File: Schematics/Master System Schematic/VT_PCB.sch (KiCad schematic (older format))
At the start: 34 parts, among them K13 Voltage Tap Relay, K14 Voltage Tap Relay, K15 Voltage Tap Relay, K16 Voltage Tap Relay, K17 Voltage Tap Relay, K18 Voltage Tap Relay, K19 Voltage Tap Relay, K20 Voltage Tap Relay, K21 Voltage Tap Relay, K22 Voltage Tap Relay

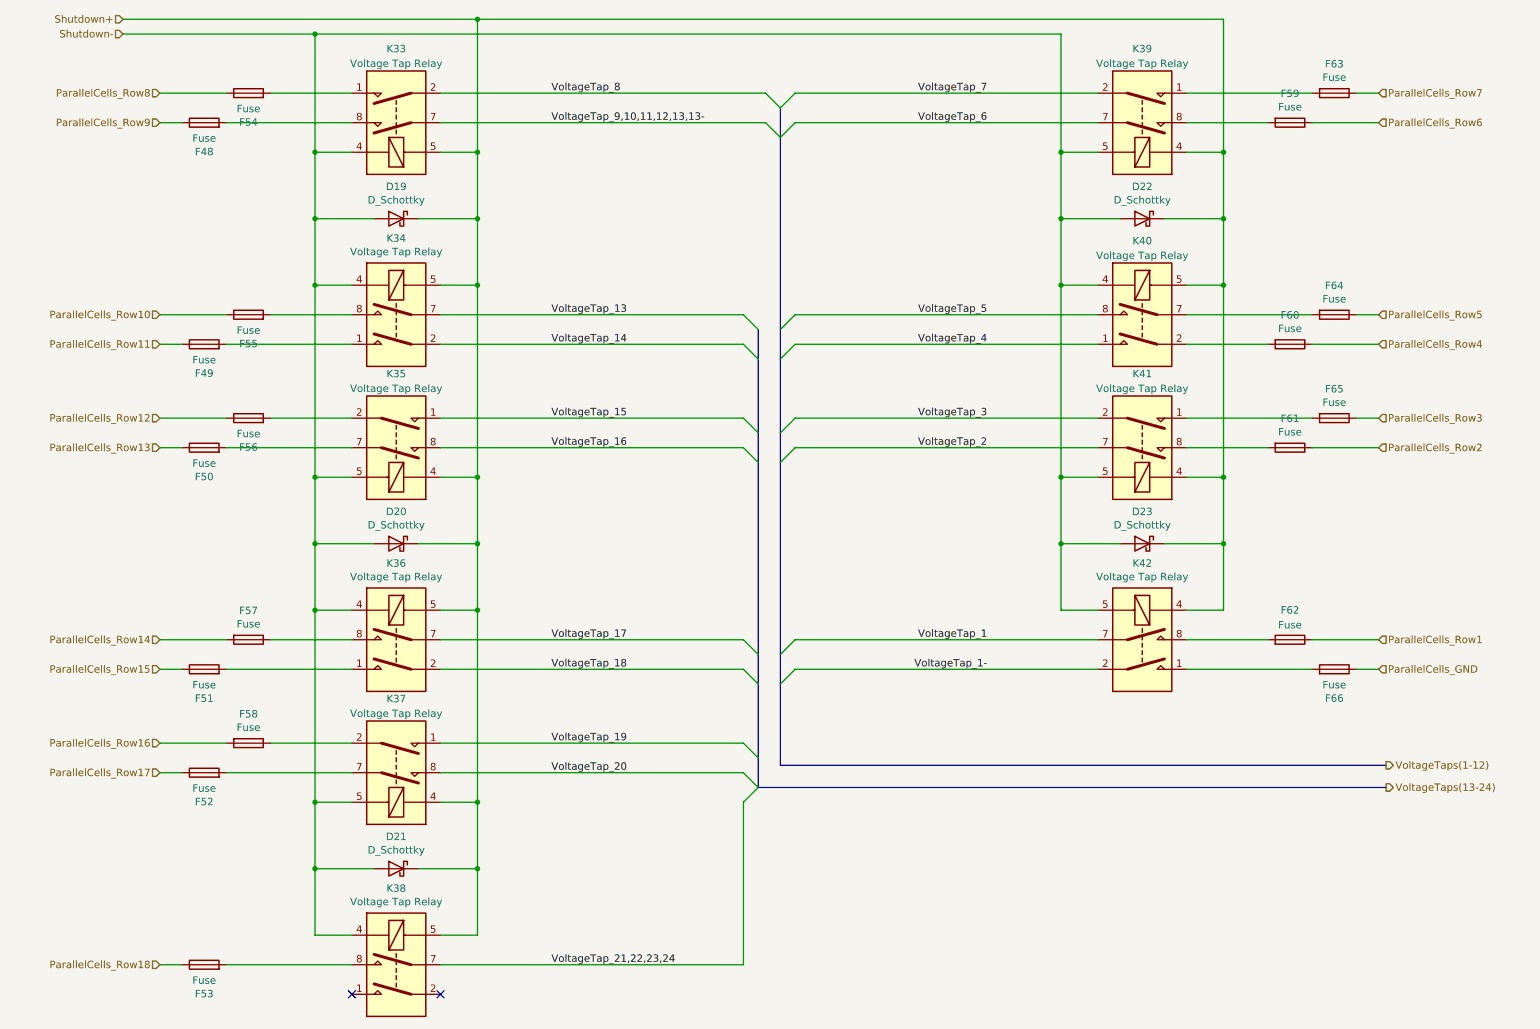
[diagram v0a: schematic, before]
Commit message: Added cooling pump off while charging functionality
>Added diode so glv battery cannot supply charging power to bms
>added pulldown resistor for charging power line to ground
>Connected charging power line to second side of cooling pump relay coil
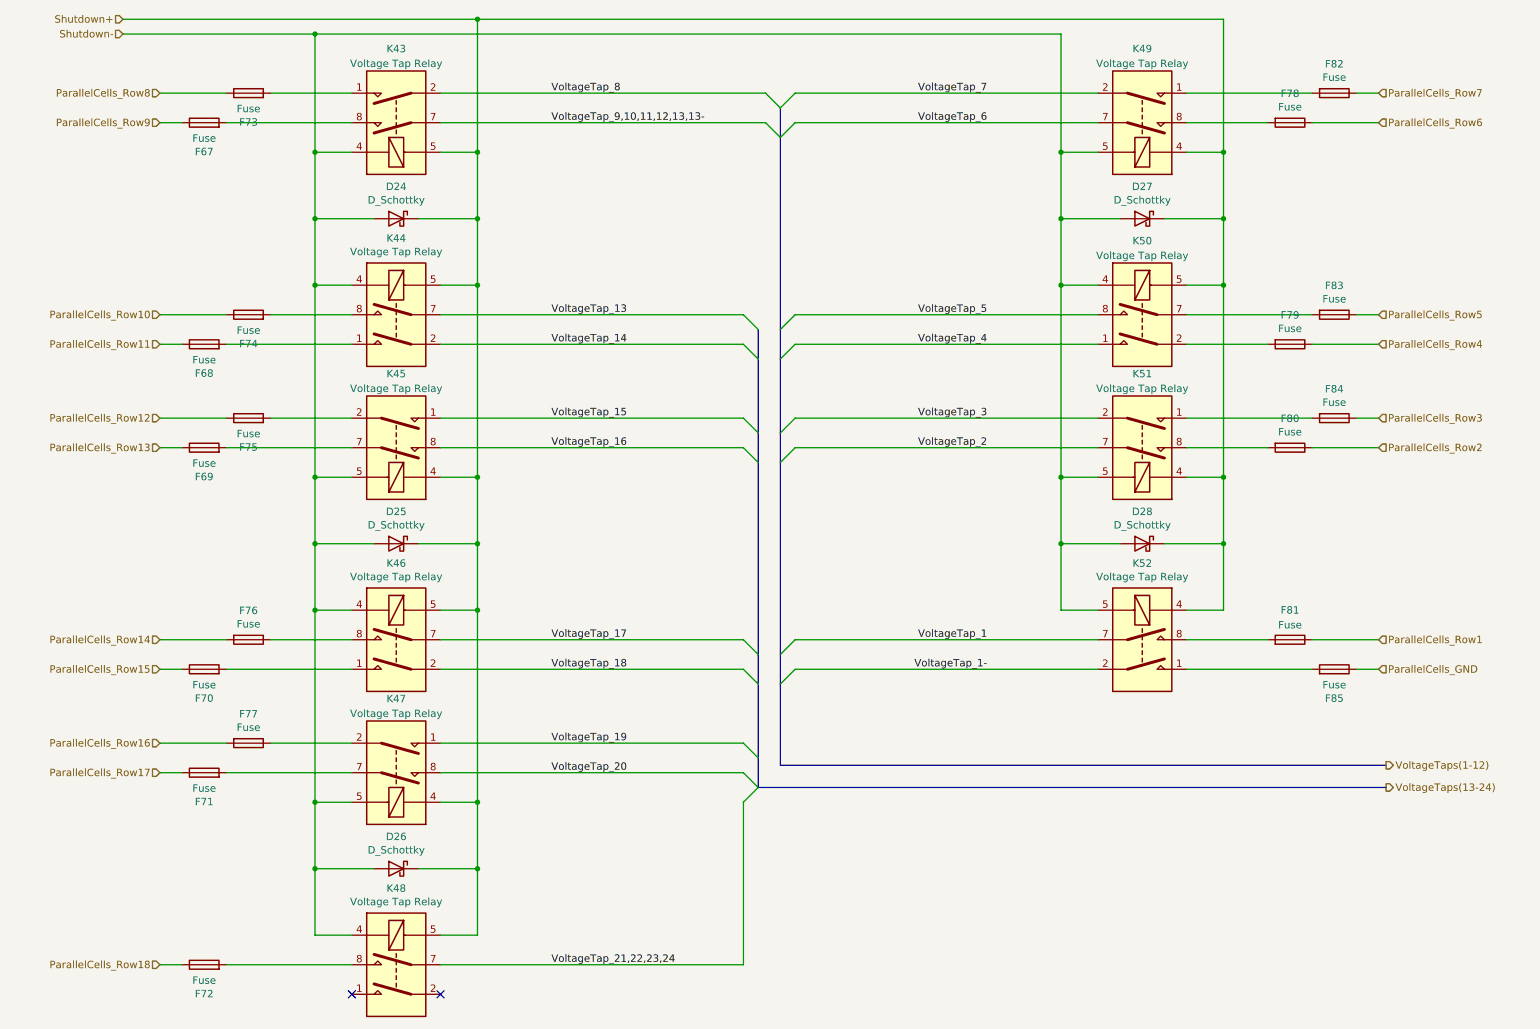
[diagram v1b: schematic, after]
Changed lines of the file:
@@
 $Descr A4 11693 8268
 encoding utf-8
-Sheet 14 21
+Sheet 15 21
 Title "Voltage Tap Connector PCB"
 Date "2020-10-16"
@@
 AR Path="/5F45B05E/605AC384/6054A887" Ref="K35"  Part="1"
 AR Path="/5F45B05E/605B3BFB/6054A887" Ref="K45"  Part="1"
-F 0 "K35" H 3450 3250 50  0000 C CNN
+F 0 "K45" H 3450 3250 50  0000 C CNN
 F 1 "Voltage Tap Relay" H 3450 3350 50  0000 C CNN
 F 2 "Relay_THT:Relay_DPST_Fujitsu_FTR-F1A" H 3450 3350 50  0001 C CNN
@@
 AR Path="/5F45B05E/605AC384/6054A88D" Ref="K36"  Part="1"
 AR Path="/5F45B05E/605B3BFB/6054A88D" Ref="K46"  Part="1"
-F 0 "K36" H 3450 5567 50  0000 C CNN
+F 0 "K46" H 3450 5567 50  0000 C CNN
 F 1 "Voltage Tap Relay" H 3450 5476 50  0000 C CNN
 F 2 "Relay_THT:Relay_DPST_Fujitsu_FTR-F1A" H 3450 4650 50  0001 C CNN
@@
 AR Path="/5F45B05E/605AC384/6054A893" Ref="K37"  Part="1"
 AR Path="/5F45B05E/605B3BFB/6054A893" Ref="K47"  Part="1"
-F 0 "K37" H 3450 5450 50  0000 C CNN
+F 0 "K47" H 3450 5450 50  0000 C CNN
 F 1 "Voltage Tap Relay" H 3450 5550 50  0000 C CNN
 F 2 "Relay_THT:Relay_DPST_Fujitsu_FTR-F1A" H 3450 5550 50  0001 C CNN
@@
 AR Path="/5F45B05E/605AC384/6057794E" Ref="F51"  Part="1"
 AR Path="/5F45B05E/605B3BFB/6057794E" Ref="F70"  Part="1"
-F 0 "F51" V 1953 5250 50  0000 C CNN
+F 0 "F70" V 1953 5250 50  0000 C CNN
 F 1 "Fuse" V 2044 5250 50  0000 C CNN
 F 2 "" V 2080 5250 50  0001 C CNN
@@
 AR Path="/5F45B05E/605AC384/60579EA8" Ref="F50"  Part="1"
 AR Path="/5F45B05E/605B3BFB/60579EA8" Ref="F69"  Part="1"
-F 0 "F50" V 1953 3750 50  0000 C CNN
+F 0 "F69" V 1953 3750 50  0000 C CNN
 F 1 "Fuse" V 2044 3750 50  0000 C CNN
 F 2 "" V 2080 3750 50  0001 C CNN
@@
 AR Path="/5F45B05E/605AC384/60579EAE" Ref="F56"  Part="1"
 AR Path="/5F45B05E/605B3BFB/60579EAE" Ref="F75"  Part="1"
-F 0 "F56" V 2253 3550 50  0000 C CNN
+F 0 "F75" V 2253 3550 50  0000 C CNN
 F 1 "Fuse" V 2344 3550 50  0000 C CNN
 F 2 "" V 2380 3550 50  0001 C CNN
@@
 AR Path="/5F45B05E/605AC384/60579EB6" Ref="F49"  Part="1"
 AR Path="/5F45B05E/605B3BFB/60579EB6" Ref="F68"  Part="1"
-F 0 "F49" V 1953 3050 50  0000 C CNN
+F 0 "F68" V 1953 3050 50  0000 C CNN
 F 1 "Fuse" V 2044 3050 50  0000 C CNN
 F 2 "" V 2080 3050 50  0001 C CNN
@@
 AR Path="/5F45B05E/605AC384/60579EBC" Ref="F55"  Part="1"
 AR Path="/5F45B05E/605B3BFB/60579EBC" Ref="F74"  Part="1"
-F 0 "F55" V 2253 2850 50  0000 C CNN
+F 0 "F74" V 2253 2850 50  0000 C CNN
 F 1 "Fuse" V 2344 2850 50  0000 C CNN
 F 2 "" V 2380 2850 50  0001 C CNN
@@
 AR Path="/5F45B05E/605AC384/6057BB2B" Ref="F48"  Part="1"
 AR Path="/5F45B05E/605B3BFB/6057BB2B" Ref="F67"  Part="1"
-F 0 "F48" V 1953 1550 50  0000 C CNN
+F 0 "F67" V 1953 1550 50  0000 C CNN
 F 1 "Fuse" V 2044 1550 50  0000 C CNN
 F 2 "" V 2080 1550 50  0001 C CNN
@@
 AR Path="/5F45B05E/605AC384/6057BB31" Ref="F54"  Part="1"
 AR Path="/5F45B05E/605B3BFB/6057BB31" Ref="F73"  Part="1"
-F 0 "F54" V 2253 1350 50  0000 C CNN
+F 0 "F73" V 2253 1350 50  0000 C CNN
 F 1 "Fuse" V 2344 1350 50  0000 C CNN
 F 2 "" V 2380 1350 50  0001 C CNN
@@
 AR Path="/5F45B05E/605AC384/6057BB39" Ref="F63"  Part="1"
 AR Path="/5F45B05E/605B3BFB/6057BB39" Ref="F82"  Part="1"
-F 0 "F63" V 9603 1350 50  0000 C CNN
+F 0 "F82" V 9603 1350 50  0000 C CNN
 F 1 "Fuse" V 9694 1350 50  0000 C CNN
 F 2 "" V 9730 1350 50  0001 C CNN
@@
 AR Path="/5F45B05E/605AC384/6057BB3F" Ref="F59"  Part="1"
 AR Path="/5F45B05E/605B3BFB/6057BB3F" Ref="F78"  Part="1"
-F 0 "F59" V 9303 1550 50  0000 C CNN
+F 0 "F78" V 9303 1550 50  0000 C CNN
 F 1 "Fuse" V 9394 1550 50  0000 C CNN
 F 2 "" V 9430 1550 50  0001 C CNN
@@
 AR Path="/5F45B05E/605AC384/6057BB47" Ref="F64"  Part="1"
 AR Path="/5F45B05E/605B3BFB/6057BB47" Ref="F83"  Part="1"
-F 0 "F64" V 9603 2850 50  0000 C CNN
+F 0 "F83" V 9603 2850 50  0000 C CNN
 F 1 "Fuse" V 9694 2850 50  0000 C CNN
 F 2 "" V 9730 2850 50  0001 C CNN
@@
 AR Path="/5F45B05E/605AC384/6057BB4D" Ref="F60"  Part="1"
 AR Path="/5F45B05E/605B3BFB/6057BB4D" Ref="F79"  Part="1"
-F 0 "F60" V 9303 3050 50  0000 C CNN
+F 0 "F79" V 9303 3050 50  0000 C CNN
 F 1 "Fuse" V 9394 3050 50  0000 C CNN
 F 2 "" V 9430 3050 50  0001 C CNN
@@
 AR Path="/5F45B05E/605AC384/6057BB55" Ref="F65"  Part="1"
 AR Path="/5F45B05E/605B3BFB/6057BB55" Ref="F84"  Part="1"
-F 0 "F65" V 9603 3550 50  0000 C CNN
+F 0 "F84" V 9603 3550 50  0000 C CNN
 F 1 "Fuse" V 9694 3550 50  0000 C CNN
 F 2 "" V 9730 3550 50  0001 C CNN
@@
 AR Path="/5F45B05E/605AC384/6057BB5B" Ref="F61"  Part="1"
 AR Path="/5F45B05E/605B3BFB/6057BB5B" Ref="F80"  Part="1"
-F 0 "F61" V 9303 3750 50  0000 C CNN
+F 0 "F80" V 9303 3750 50  0000 C CNN
 F 1 "Fuse" V 9394 3750 50  0000 C CNN
 F 2 "" V 9430 3750 50  0001 C CNN
@@
 AR Path="/5F45B05E/605AC384/6057D363" Ref="F66"  Part="1"
 AR Path="/5F45B05E/605B3BFB/6057D363" Ref="F85"  Part="1"
-F 0 "F66" V 9603 5250 50  0000 C CNN
+F 0 "F85" V 9603 5250 50  0000 C CNN
 F 1 "Fuse" V 9694 5250 50  0000 C CNN
 F 2 "" V 9730 5250 50  0001 C CNN
@@
 AR Path="/5F45B05E/605AC384/6057D369" Ref="F62"  Part="1"
 AR Path="/5F45B05E/605B3BFB/6057D369" Ref="F81"  Part="1"
-F 0 "F62" V 9700 5050 50  0000 C CNN
+F 0 "F81" V 9700 5050 50  0000 C CNN
 F 1 "Fuse" V 9600 5050 50  0000 C CNN
 F 2 "" V 9430 5050 50  0001 C CNN
@@
 AR Path="/5F45B05E/605AC384/5FB6A078" Ref="D19"  Part="1"
 AR Path="/5F45B05E/605B3BFB/5FB6A078" Ref="D24"  Part="1"
-F 0 "D19" H 3450 2417 50  0000 C CNN
+F 0 "D24" H 3450 2417 50  0000 C CNN
 F 1 "D_Schottky" H 3450 2326 50  0000 C CNN
 F 2 "" H 3450 2200 50  0001 C CNN
@@
 AR Path="/5F45B05E/605AC384/5FB74EA7" Ref="D20"  Part="1"
 AR Path="/5F45B05E/605B3BFB/5FB74EA7" Ref="D25"  Part="1"
-F 0 "D20" H 3450 4617 50  0000 C CNN
+F 0 "D25" H 3450 4617 50  0000 C CNN
 F 1 "D_Schottky" H 3450 4526 50  0000 C CNN
 F 2 "" H 3450 4400 50  0001 C CNN
@@
 AR Path="/5F45B05E/605AC384/5FB78242" Ref="D23"  Part="1"
 AR Path="/5F45B05E/605B3BFB/5FB78242" Ref="D28"  Part="1"
-F 0 "D23" H 8500 4617 50  0000 C CNN
+F 0 "D28" H 8500 4617 50  0000 C CNN
 F 1 "D_Schottky" H 8500 4526 50  0000 C CNN
 F 2 "" H 8500 4400 50  0001 C CNN
@@
 AR Path="/5F45B05E/605AC384/5FB7A02F" Ref="D22"  Part="1"
 AR Path="/5F45B05E/605B3BFB/5FB7A02F" Ref="D27"  Part="1"
-F 0 "D22" H 8500 2417 50  0000 C CNN
+F 0 "D27" H 8500 2417 50  0000 C CNN
 F 1 "D_Schottky" H 8500 2326 50  0000 C CNN
 F 2 "" H 8500 2200 50  0001 C CNN
@@
 AR Path="/5F45B05E/605AC384/5FBDF245" Ref="K33"  Part="1"
 AR Path="/5F45B05E/605B3BFB/5FBDF245" Ref="K43"  Part="1"
-F 0 "K33" H 3450 1050 50  0000 C CNN
+F 0 "K43" H 3450 1050 50  0000 C CNN
 F 1 "Voltage Tap Relay" H 3450 1150 50  0000 C CNN
 F 2 "Relay_THT:Relay_DPST_Fujitsu_FTR-F1A" H 3450 1150 50  0001 C CNN
@@
 AR Path="/5F45B05E/605AC384/5FBDF24B" Ref="K39"  Part="1"
 AR Path="/5F45B05E/605B3BFB/5FBDF24B" Ref="K49"  Part="1"
-F 0 "K39" H 8500 1050 50  0000 C CNN
+F 0 "K49" H 8500 1050 50  0000 C CNN
 F 1 "Voltage Tap Relay" H 8500 1150 50  0000 C CNN
 F 2 "Relay_THT:Relay_DPST_Fujitsu_FTR-F1A" H 8500 1150 50  0001 C CNN
@@
 AR Path="/5F45B05E/605AC384/5FBDF251" Ref="K40"  Part="1"
 AR Path="/5F45B05E/605B3BFB/5FBDF251" Ref="K50"  Part="1"
-F 0 "K40" H 8500 3350 50  0000 C CNN
+F 0 "K50" H 8500 3350 50  0000 C CNN
 F 1 "Voltage Tap Relay" H 8500 3250 50  0000 C CNN
 F 2 "Relay_THT:Relay_DPST_Fujitsu_FTR-F1A" H 8500 2450 50  0001 C CNN
@@
 AR Path="/5F45B05E/605AC384/5FBDF257" Ref="K42"  Part="1"
 AR Path="/5F45B05E/605B3BFB/5FBDF257" Ref="K52"  Part="1"
-F 0 "K42" H 8500 5567 50  0000 C CNN
+F 0 "K52" H 8500 5567 50  0000 C CNN
 F 1 "Voltage Tap Relay" H 8500 5476 50  0000 C CNN
 F 2 "Relay_THT:Relay_DPST_Fujitsu_FTR-F1A" H 8500 4650 50  0001 C CNN
@@
 AR Path="/5F45B05E/605AC384/5FBDF25D" Ref="K41"  Part="1"
 AR Path="/5F45B05E/605B3BFB/5FBDF25D" Ref="K51"  Part="1"
-F 0 "K41" H 8500 3250 50  0000 C CNN
+F 0 "K51" H 8500 3250 50  0000 C CNN
 F 1 "Voltage Tap Relay" H 8500 3350 50  0000 C CNN
 F 2 "Relay_THT:Relay_DPST_Fujitsu_FTR-F1A" H 8500 3350 50  0001 C CNN
@@
 AR Path="/5F45B05E/605AC384/60548E5D" Ref="K34"  Part="1"
 AR Path="/5F45B05E/605B3BFB/60548E5D" Ref="K44"  Part="1"
-F 0 "K34" H 3450 3367 50  0000 C CNN
+F 0 "K44" H 3450 3367 50  0000 C CNN
 F 1 "Voltage Tap Relay" H 3450 3276 50  0000 C CNN
 F 2 "Relay_THT:Relay_DPST_Fujitsu_FTR-F1A" H 3450 2450 50  0001 C CNN
@@
 AR Path="/5F45B05E/605AC384/5FB76776" Ref="D21"  Part="1"
 AR Path="/5F45B05E/605B3BFB/5FB76776" Ref="D26"  Part="1"
-F 0 "D21" H 3450 6817 50  0000 C CNN
+F 0 "D26" H 3450 6817 50  0000 C CNN
 F 1 "D_Schottky" H 3450 6726 50  0000 C CNN
 F 2 "" H 3450 6600 50  0001 C CNN
@@
 AR Path="/5F45B05E/605AC384/5FC1EEB9" Ref="F53"  Part="1"
 AR Path="/5F45B05E/605B3BFB/5FC1EEB9" Ref="F72"  Part="1"
-F 0 "F53" V 1953 7250 50  0000 C CNN
+F 0 "F72" V 1953 7250 50  0000 C CNN
 F 1 "Fuse" V 2044 7250 50  0000 C CNN
 F 2 "" V 2080 7250 50  0001 C CNN
@@
 AR Path="/5F45B05E/605AC384/6054A899" Ref="K38"  Part="1"
 AR Path="/5F45B05E/605B3BFB/6054A899" Ref="K48"  Part="1"
-F 0 "K38" H 3450 7767 50  0000 C CNN
+F 0 "K48" H 3450 7767 50  0000 C CNN
 F 1 "Voltage Tap Relay" H 3450 7676 50  0000 C CNN
 F 2 "Relay_THT:Relay_DPST_Fujitsu_FTR-F1A" H 3450 6850 50  0001 C CNN
@@
 AR Path="/5F45B05E/605AC384/5FD0ECB2" Ref="F58"  Part="1"
 AR Path="/5F45B05E/605B3BFB/5FD0ECB2" Ref="F77"  Part="1"
-F 0 "F58" V 2253 5750 50  0000 C CNN
+F 0 "F77" V 2253 5750 50  0000 C CNN
 F 1 "Fuse" V 2344 5750 50  0000 C CNN
 F 2 "" V 2380 5750 50  0001 C CNN
@@
 AR Path="/5F45B05E/605AC384/5FD12DBC" Ref="F57"  Part="1"
 AR Path="/5F45B05E/605B3BFB/5FD12DBC" Ref="F76"  Part="1"
-F 0 "F57" V 2253 5050 50  0000 C CNN
+F 0 "F76" V 2253 5050 50  0000 C CNN
 F 1 "Fuse" V 2344 5050 50  0000 C CNN
 F 2 "" V 2380 5050 50  0001 C CNN
@@
 AR Path="/5F45B05E/605AC384/5FD210E5" Ref="F52"  Part="1"
 AR Path="/5F45B05E/605B3BFB/5FD210E5" Ref="F71"  Part="1"
-F 0 "F52" V 1953 5950 50  0000 C CNN
+F 0 "F71" V 1953 5950 50  0000 C CNN
 F 1 "Fuse" V 2044 5950 50  0000 C CNN
 F 2 "" V 2080 5950 50  0001 C CNN
